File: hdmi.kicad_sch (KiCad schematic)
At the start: 50 parts, among them J2 46756-1001

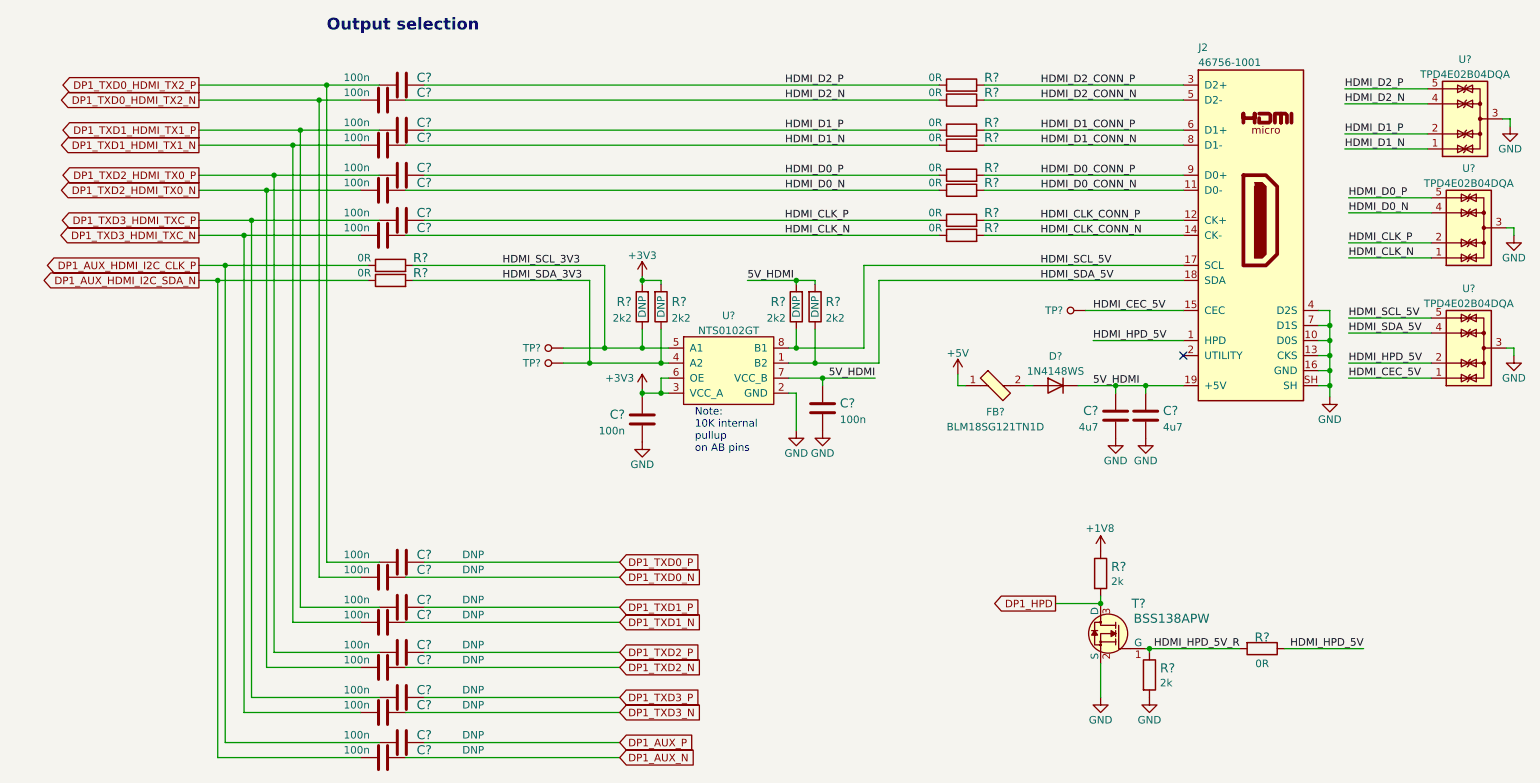
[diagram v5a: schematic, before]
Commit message: Replace HPD voltage converter with parts from global library
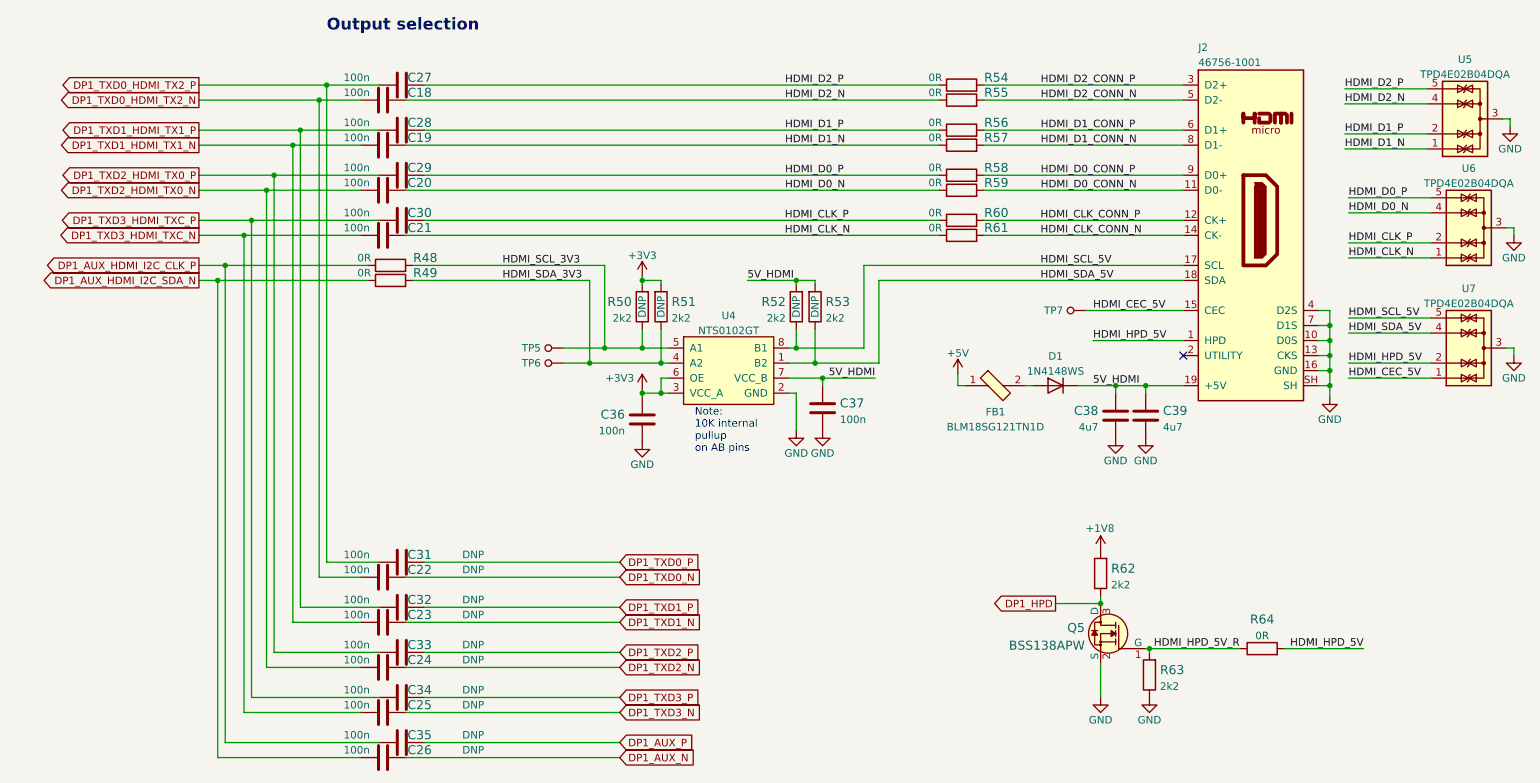
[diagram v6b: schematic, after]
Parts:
- removed R? (x2): R_2k_0402, jetson-nano-baseboard-footprints:0402-res, symbol jetson-nano-baseboard:R_2k_0402
- removed R?: R_0R_0402, jetson-nano-baseboard-footprints:0402-res, symbol jetson-nano-baseboard:R_0R_0402
- removed T?: BSS138APW, jetson-nano-baseboard-footprints:SC70-3, symbol jetson-nano-baseboard:BSS138APW
- added Q5: BSS138APW, antmicro-footprints:SC70-3, symbol antmicroTransistorsFETsMOSFETsSingle:BSS138APW
- added R62, R63: R_2k2_0402, antmicro-footprints:0402-res, symbol antmicroResistors0402:R_2k2_0402
- added R64: R_0R_0402, antmicro-footprints:0402-res, symbol antmicroResistors0402:R_0R_0402
- gave numbers to parts that had none: 45
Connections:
- net +1V8: now also R62.2
- net DP1_HPD: now also Q5.3 (D), R62.1
- net GND: now also Q5.2 (S), R63.1
- net HDMI_HPD_5V: now also R64.2
- net HDMI_HPD_5V_R: now also Q5.1 (G), R63.2, R64.1

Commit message: Unify reference designator and value text size, minor improvements on som subsheet
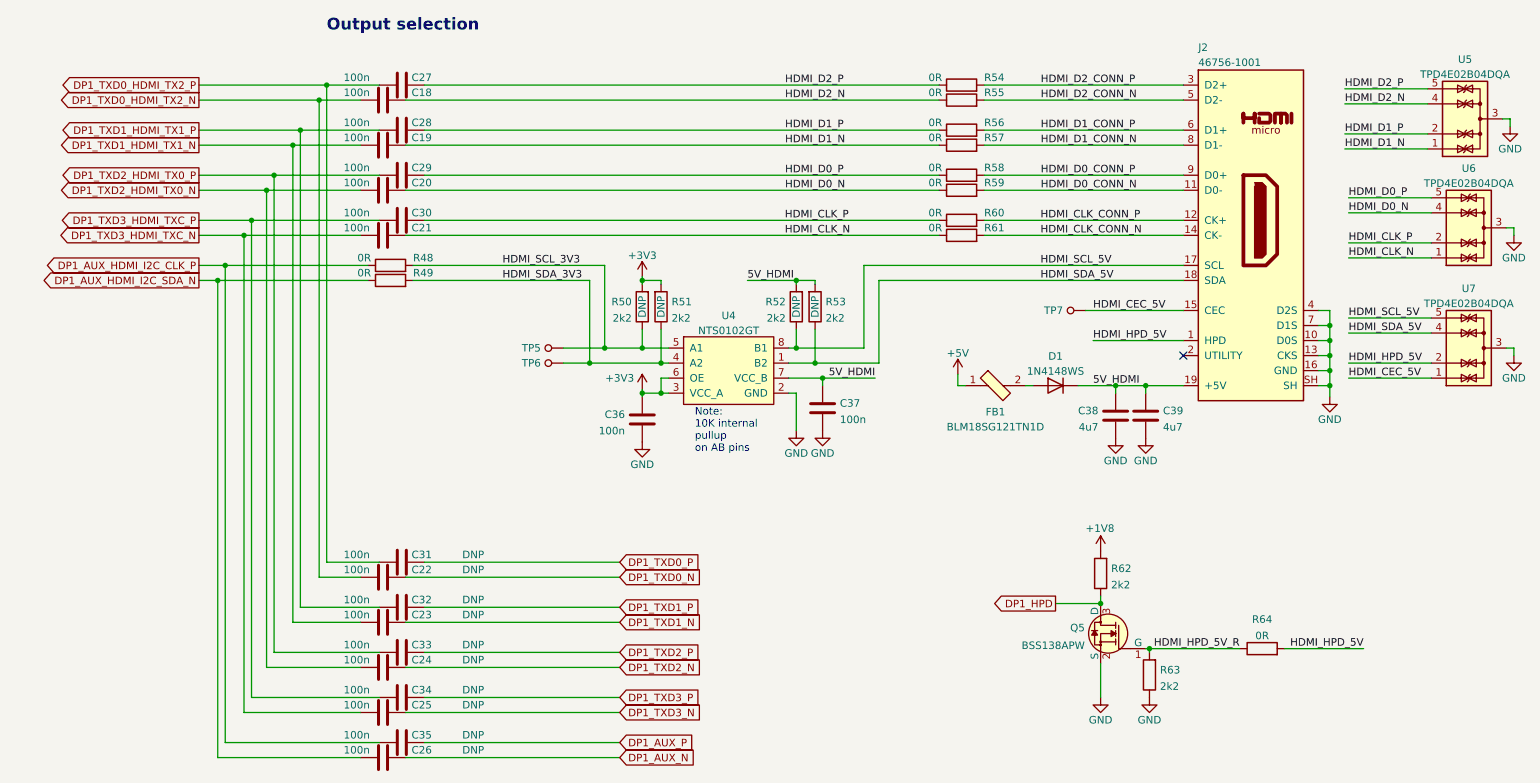
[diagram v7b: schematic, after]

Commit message: Reannotate parts
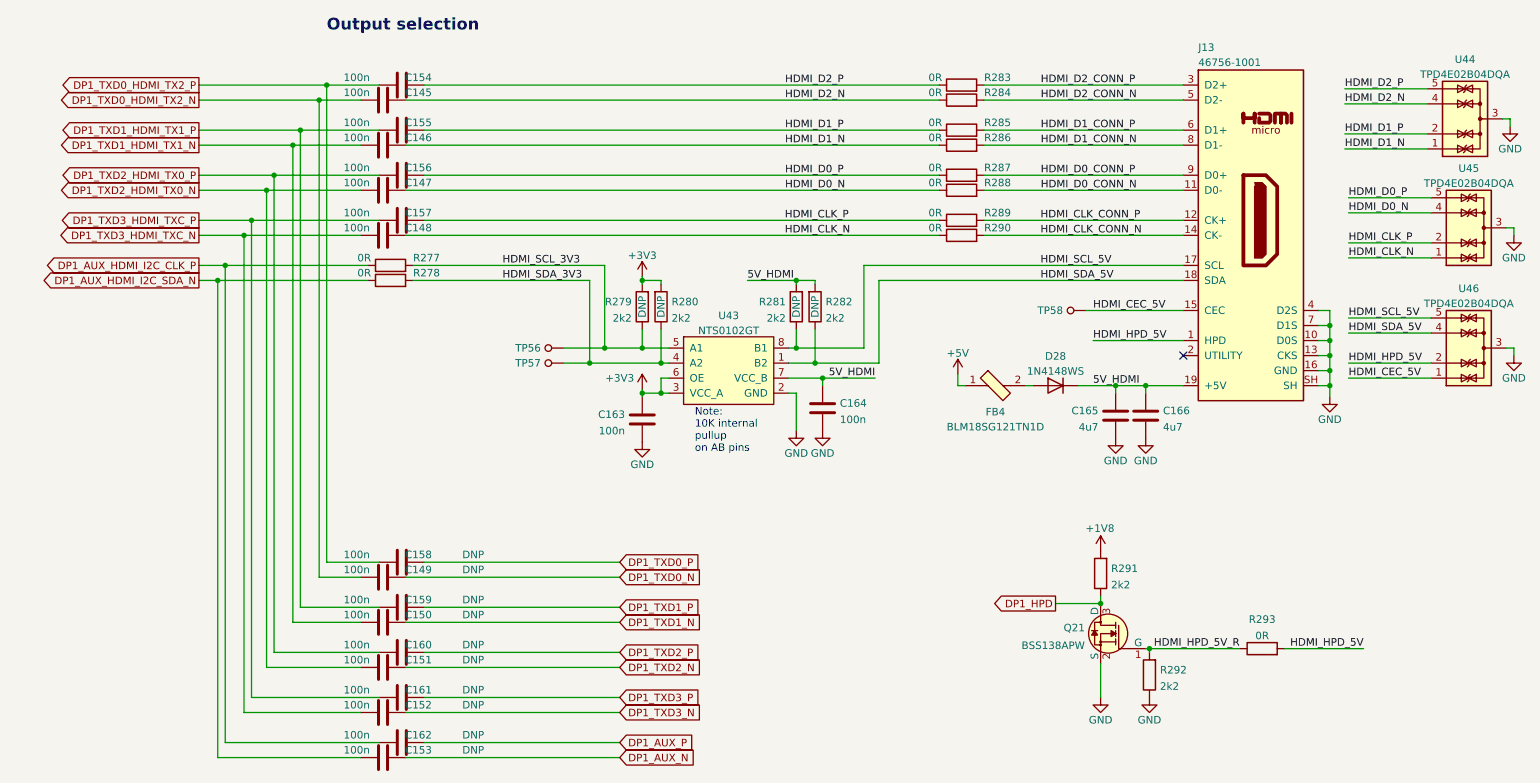
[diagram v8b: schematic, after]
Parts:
- renumbered C18 to C145, C19 to C146, C20 to C147, C21 to C148, C22 to C149, C23 to C150, C24 to C151, C25 to C152, C26 to C153, C27 to C154, C28 to C155, C29 to C156, C30 to C157, C31 to C158, C32 to C159, C33 to C160, C34 to C161, C35 to C162, C36 to C163, C37 to C164, C38 to C165, C39 to C166, D1 to D28, FB1 to FB4, J2 to J13, Q5 to Q21, R48 to R277, R49 to R278, R50 to R279, R51 to R280, R52 to R281, R53 to R282, R54 to R283, R55 to R284, R56 to R285, R57 to R286, R58 to R287, R59 to R288, R60 to R289, R61 to R290, R62 to R291, R63 to R292, R64 to R293, TP5 to TP56, TP6 to TP57, TP7 to TP58, U4 to U43, U5 to U44, U6 to U45, U7 to U46
